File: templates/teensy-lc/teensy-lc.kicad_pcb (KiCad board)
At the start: 2 copper layers, 25.4 x 41.9 mm, 2 parts, among them J1 TEENSY LC

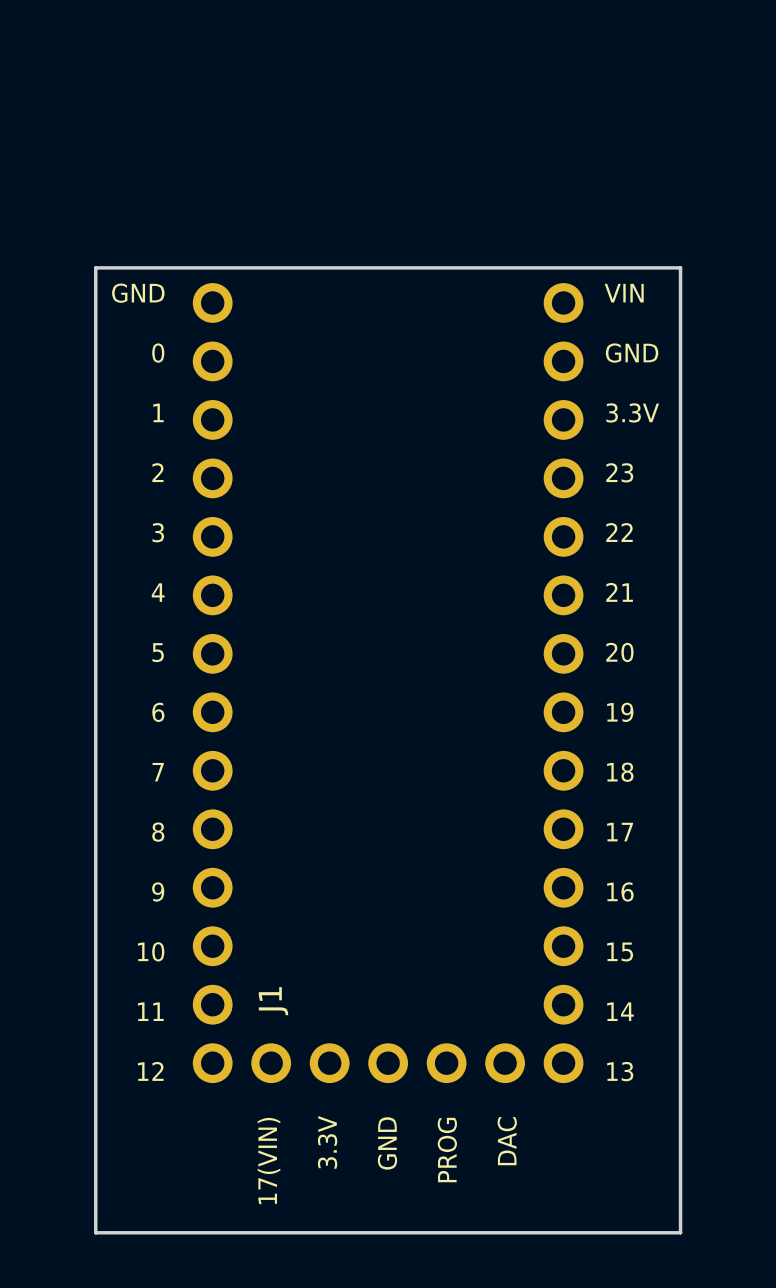
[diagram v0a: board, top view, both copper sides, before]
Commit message: Made the Teensy LC template independent.
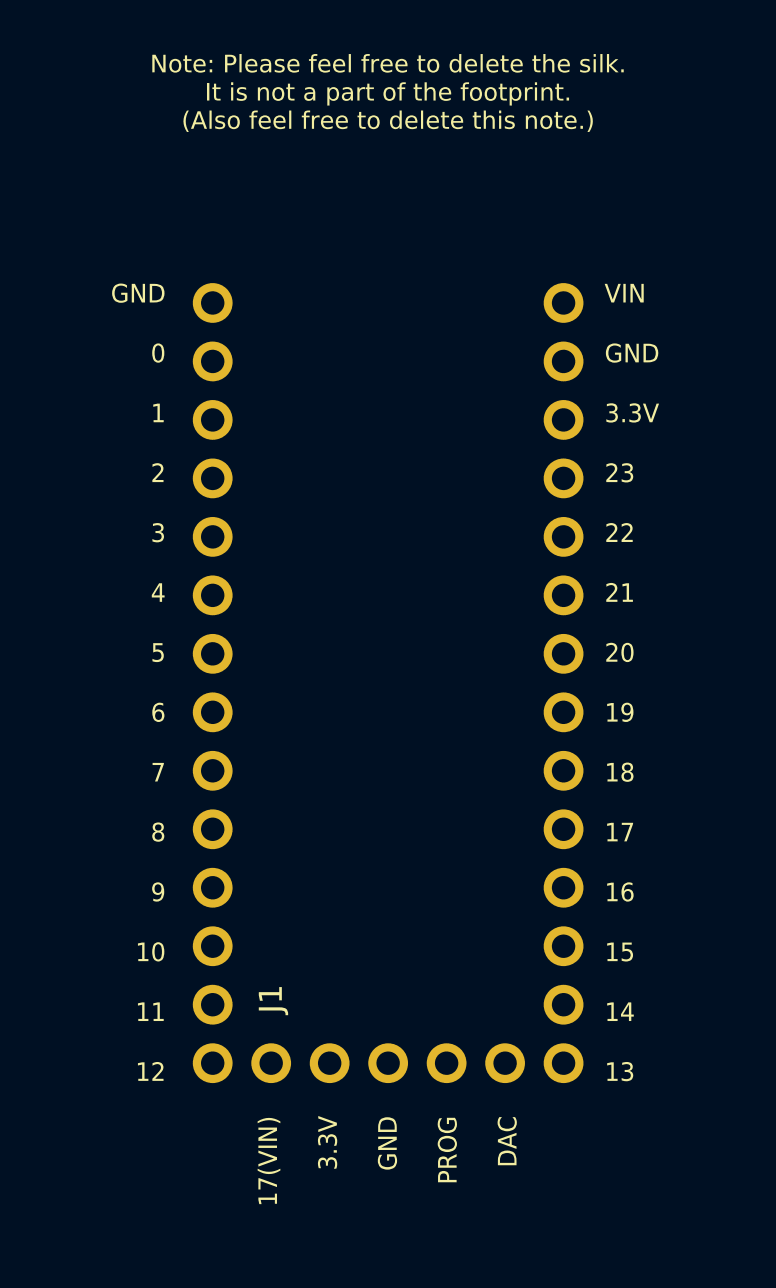
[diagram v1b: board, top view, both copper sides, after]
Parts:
- removed REF**: Symbol_OSHW-Logo_SilkScreen, Wickerlib:Symbol_OSHW-Logo_SilkScreen
- J1: footprint Wickerlib:TEENSY-LC -> TEENSY-LC
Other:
- board outline removed
- board text added: "Note: Please feel free to delete the silk. It is not a part of the footprint. (Also feel free to delete this note.)"
- board text removed: "TEMPLATE TEST BOARD"
